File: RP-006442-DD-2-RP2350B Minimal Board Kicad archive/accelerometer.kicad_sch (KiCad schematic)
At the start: 4 parts, among them U13 MMA8451QR1

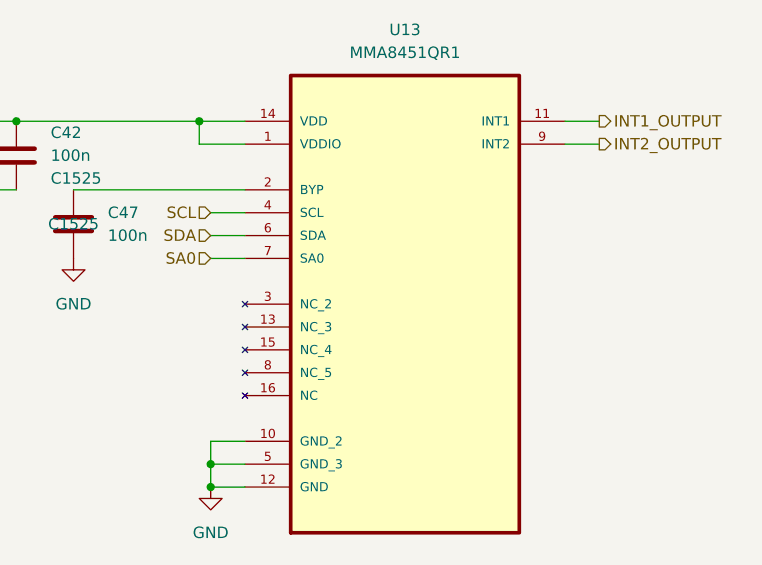
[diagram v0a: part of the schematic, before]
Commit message: Added LCSC number to accelerometer
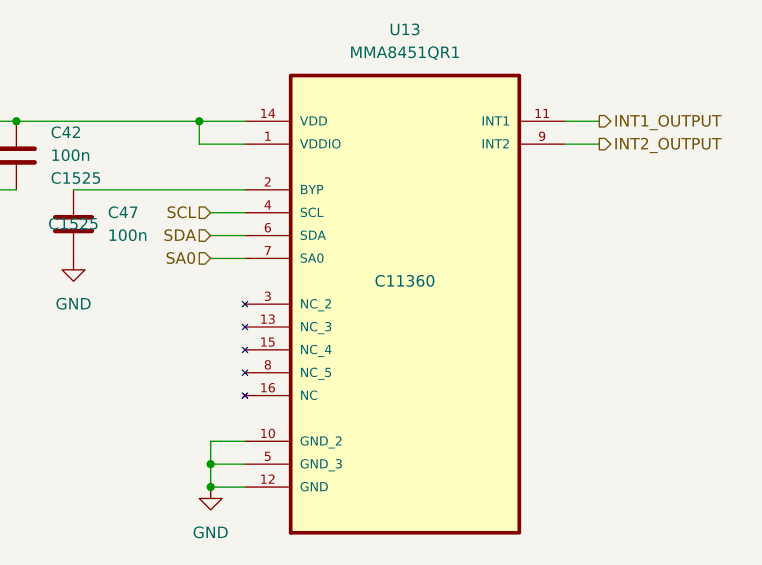
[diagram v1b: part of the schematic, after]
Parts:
- U13: LCSC (none) -> C11360
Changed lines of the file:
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@@
+			)
+		)
+		(property "LCSC" "C11360"
+			(at 143.51 76.2 0)
+			(effects
+				(font
+					(size 1.27 1.27)
+				)
 			)
 		)

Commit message: Created Figures
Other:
- note removed: "Pin CS is SPI enable 1: I2C enable/SPI idle 0: SPI enable/I2C disabled"
- moved on the sheet: C42, C45, C47, U13
